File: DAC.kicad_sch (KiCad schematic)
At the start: 27 parts, among them J18 DAC_I2S, J19 DAC_OUT, J20 DAC_Amplified, J21 DAC_Amplified, J26 DAC_I2S, U6 PCM5100APW, U8 TL072

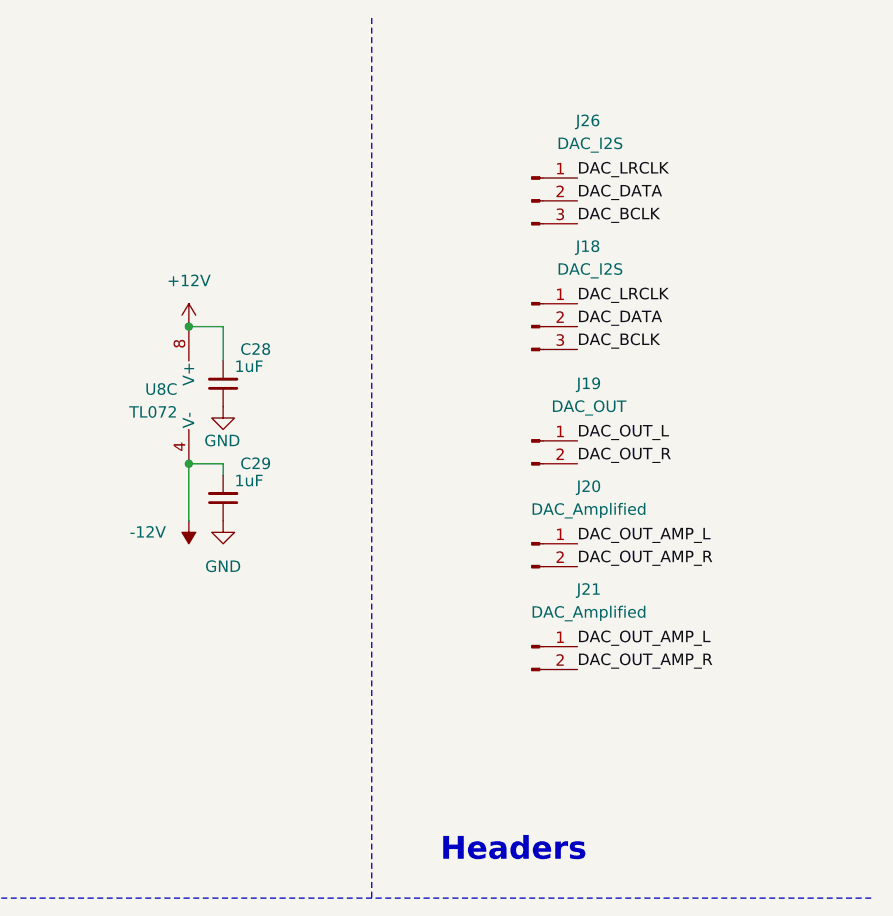
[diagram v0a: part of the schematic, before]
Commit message: Layout tweaks
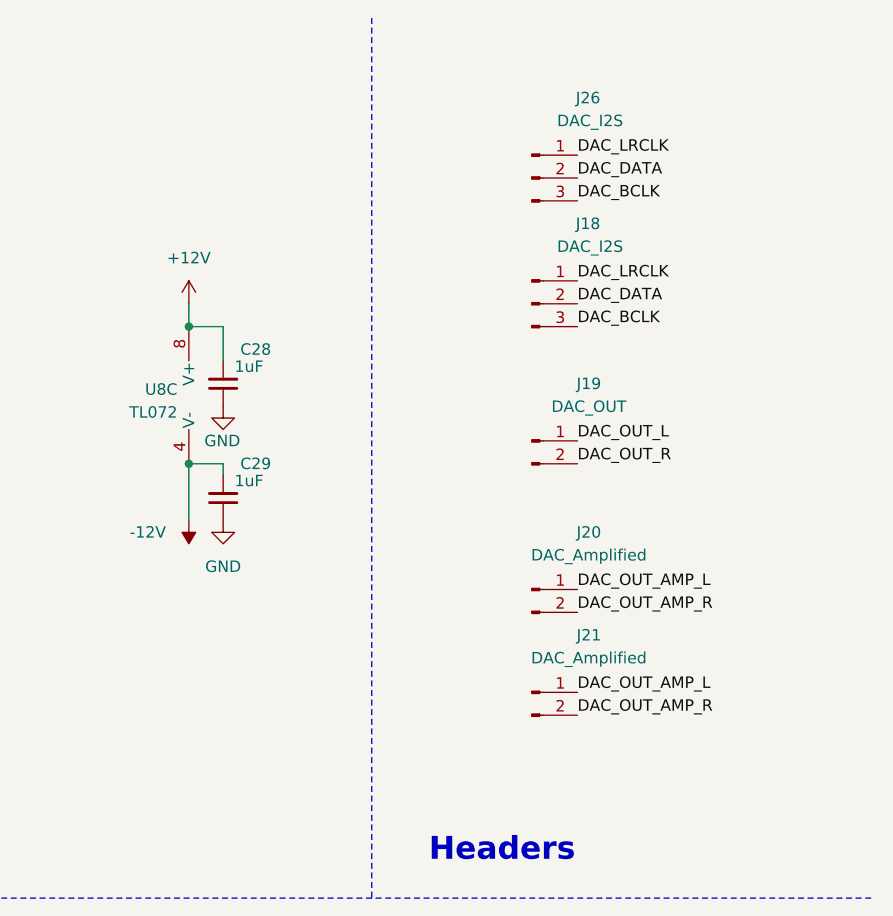
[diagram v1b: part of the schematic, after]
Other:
- moved on the sheet: J18, J20, J21, J26
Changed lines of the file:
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@@
+    (stroke (width 0) (type default))
+  )
+  (wire (pts (xy 208.28 44.45) (xy 208.28 46.99))
     (stroke (width 0) (type default))
   )
@@
     (stroke (width 0) (type default))
   )
-  (text "Headers" (at 236.22 106.68 0)
+  (text "Headers" (at 234.95 106.68 0)
     (effects (font (size 2.54 2.54) (thickness 0.508) bold) (justify left bottom))
   )
@@
     (effects (font (size 1.27 1.27)) (justify right bottom))
   )
-  (label "DAC_BCLK" (at 251.46 49.53 0) (fields_autoplaced)
-    (effects (font (size 1.27 1.27)) (justify left bottom))
-  )
-  (label "DAC_LRCLK" (at 251.46 30.48 0) (fields_autoplaced)
-    (effects (font (size 1.27 1.27)) (justify left bottom))
-  )
-  (label "DAC_DATA" (at 251.46 33.02 0) (fields_autoplaced)
+  (label "DAC_BCLK" (at 251.46 46.99 0) (fields_autoplaced)
+    (effects (font (size 1.27 1.27)) (justify left bottom))
+  )
+  (label "DAC_LRCLK" (at 251.46 27.94 0) (fields_autoplaced)
+    (effects (font (size 1.27 1.27)) (justify left bottom))
+  )
+  (label "DAC_DATA" (at 251.46 30.48 0) (fields_autoplaced)
     (effects (font (size 1.27 1.27)) (justify left bottom))
   )
@@
     (effects (font (size 1.27 1.27)) (justify right bottom))
   )
-  (label "DAC_OUT_AMP_R" (at 251.46 73.66 0) (fields_autoplaced)
+  (label "DAC_OUT_AMP_R" (at 251.46 78.74 0) (fields_autoplaced)
     (effects (font (size 1.27 1.27)) (justify left bottom))
   )
@@
     (effects (font (size 1.27 1.27)) (justify left bottom))
   )
-  (label "DAC_DATA" (at 251.46 46.99 0) (fields_autoplaced)
+  (label "DAC_DATA" (at 251.46 44.45 0) (fields_autoplaced)
     (effects (font (size 1.27 1.27)) (justify left bottom))
   )
@@
     (effects (font (size 1.27 1.27)) (justify right bottom))
   )
-  (label "DAC_OUT_AMP_R" (at 251.46 85.09 0) (fields_autoplaced)
-    (effects (font (size 1.27 1.27)) (justify left bottom))
-  )
-  (label "DAC_BCLK" (at 251.46 35.56 0) (fields_autoplaced)
-    (effects (font (size 1.27 1.27)) (justify left bottom))
-  )
-  (label "DAC_OUT_AMP_L" (at 251.46 71.12 0) (fields_autoplaced)
+  (label "DAC_OUT_AMP_R" (at 251.46 90.17 0) (fields_autoplaced)
+    (effects (font (size 1.27 1.27)) (justify left bottom))
+  )
+  (label "DAC_BCLK" (at 251.46 33.02 0) (fields_autoplaced)
+    (effects (font (size 1.27 1.27)) (justify left bottom))
+  )
+  (label "DAC_OUT_AMP_L" (at 251.46 76.2 0) (fields_autoplaced)
     (effects (font (size 1.27 1.27)) (justify left bottom))
   )
@@
     (effects (font (size 1.27 1.27)) (justify right bottom))
   )
-  (label "DAC_OUT_AMP_L" (at 251.46 82.55 0) (fields_autoplaced)
+  (label "DAC_OUT_AMP_L" (at 251.46 87.63 0) (fields_autoplaced)
     (effects (font (size 1.27 1.27)) (justify left bottom))
   )
@@
     (effects (font (size 1.27 1.27)) (justify left bottom))
   )
-  (label "DAC_LRCLK" (at 251.46 44.45 0) (fields_autoplaced)
+  (label "DAC_LRCLK" (at 251.46 41.91 0) (fields_autoplaced)
     (effects (font (size 1.27 1.27)) (justify left bottom))
   )
@@
     )
   )
-  (symbol (lib_id "Connector:Conn_01x03_Pin") (at 246.38 33.02 0) (unit 1)
-    (in_bom yes) (on_board yes) (dnp no)
-    (property "Reference" "J26" (at 254 24.13 0)
+  (symbol (lib_id "Connector:Conn_01x03_Pin") (at 246.38 30.48 0) (unit 1)
+    (in_bom yes) (on_board yes) (dnp no)
+    (property "Reference" "J26" (at 254 21.59 0)
       (effects (font (size 1.27 1.27)) (justify right))
     )
-    (property "Value" "DAC_I2S" (at 256.54 26.67 0)
+    (property "Value" "DAC_I2S" (at 256.54 24.13 0)
       (effects (font (size 1.27 1.27)) (justify right))
     )
-    (property "Footprint" "Connector_PinSocket_2.54mm:PinSocket_1x03_P2.54mm_Vertical" (at 246.38 33.02 0)
-      (effects (font (size 1.27 1.27)) hide)
-    )
-    (property "Datasheet" "~" (at 246.38 33.02 0)
+    (property "Footprint" "Connector_PinSocket_2.54mm:PinSocket_1x03_P2.54mm_Vertical" (at 246.38 30.48 0)
+      (effects (font (size 1.27 1.27)) hide)
+    )
+    (property "Datasheet" "~" (at 246.38 30.48 0)
       (effects (font (size 1.27 1.27)) hide)
     )
@@
     )
   )
-  (symbol (lib_id "Connector:Conn_01x02_Pin") (at 246.38 71.12 0) (unit 1)
-    (in_bom yes) (on_board yes) (dnp no)
-    (property "Reference" "J20" (at 252.73 64.77 0)
-      (effects (font (size 1.27 1.27)))
-    )
-    (property "Value" "DAC_Amplified" (at 252.73 67.31 0)
-      (effects (font (size 1.27 1.27)))
-    )
-    (property "Footprint" "Connector_PinSocket_2.54mm:PinSocket_1x02_P2.54mm_Vertical" (at 246.38 71.12 0)
-      (effects (font (size 1.27 1.27)) hide)
-    )
-    (property "Datasheet" "~" (at 246.38 71.12 0)
+  (symbol (lib_id "Connector:Conn_01x02_Pin") (at 246.38 76.2 0) (unit 1)
+    (in_bom yes) (on_board yes) (dnp no)
+    (property "Reference" "J20" (at 252.73 69.85 0)
+      (effects (font (size 1.27 1.27)))
+    )
+    (property "Value" "DAC_Amplified" (at 252.73 72.39 0)
+      (effects (font (size 1.27 1.27)))
+    )
+    (property "Footprint" "Connector_PinSocket_2.54mm:PinSocket_1x02_P2.54mm_Vertical" (at 246.38 76.2 0)
+      (effects (font (size 1.27 1.27)) hide)
+    )
+    (property "Datasheet" "~" (at 246.38 76.2 0)
       (effects (font (size 1.27 1.27)) hide)
     )
@@
     )
   )
-  (symbol (lib_id "power:+12V") (at 208.28 46.99 0) (unit 1)
+  (symbol (lib_id "power:+12V") (at 208.28 44.45 0) (unit 1)
     (in_bom yes) (on_board yes) (dnp no) (fields_autoplaced)
-    (property "Reference" "#PWR067" (at 208.28 50.8 0)
-      (effects (font (size 1.27 1.27)) hide)
-    )
-    (property "Value" "+12V" (at 208.28 41.91 0)
-      (effects (font (size 1.27 1.27)))
-    )
-    (property "Footprint" "" (at 208.28 46.99 0)
-      (effects (font (size 1.27 1.27)) hide)
-    )
-    (property "Datasheet" "" (at 208.28 46.99 0)
+    (property "Reference" "#PWR067" (at 208.28 48.26 0)
+      (effects (font (size 1.27 1.27)) hide)
+    )
+    (property "Value" "+12V" (at 208.28 39.37 0)
+      (effects (font (size 1.27 1.27)))
+    )
+    (property "Footprint" "" (at 208.28 44.45 0)
+      (effects (font (size 1.27 1.27)) hide)
+    )
+    (property "Datasheet" "" (at 208.28 44.45 0)
       (effects (font (size 1.27 1.27)) hide)
     )
@@
     )
   )
-  (symbol (lib_id "Connector:Conn_01x02_Pin") (at 246.38 82.55 0) (unit 1)
-    (in_bom yes) (on_board yes) (dnp no)
-    (property "Reference" "J21" (at 252.73 76.2 0)
-      (effects (font (size 1.27 1.27)))
-    )
-    (property "Value" "DAC_Amplified" (at 252.73 78.74 0)
-      (effects (font (size 1.27 1.27)))
-    )
-    (property "Footprint" "Connector_PinHeader_2.54mm:PinHeader_1x02_P2.54mm_Vertical" (at 246.38 82.55 0)
-      (effects (font (size 1.27 1.27)) hide)
-    )
-    (property "Datasheet" "~" (at 246.38 82.55 0)
+  (symbol (lib_id "Connector:Conn_01x02_Pin") (at 246.38 87.63 0) (unit 1)
+    (in_bom yes) (on_board yes) (dnp no)
+    (property "Reference" "J21" (at 252.73 81.28 0)
+      (effects (font (size 1.27 1.27)))
+    )
+    (property "Value" "DAC_Amplified" (at 252.73 83.82 0)
+      (effects (font (size 1.27 1.27)))
+    )
+    (property "Footprint" "Connector_PinHeader_2.54mm:PinHeader_1x02_P2.54mm_Vertical" (at 246.38 87.63 0)
+      (effects (font (size 1.27 1.27)) hide)
+    )
+    (property "Datasheet" "~" (at 246.38 87.63 0)
       (effects (font (size 1.27 1.27)) hide)
     )
@@
     )
   )
-  (symbol (lib_id "Connector:Conn_01x03_Pin") (at 246.38 46.99 0) (unit 1)
-    (in_bom yes) (on_board yes) (dnp no)
-    (property "Reference" "J18" (at 254 38.1 0)
+  (symbol (lib_id "Connector:Conn_01x03_Pin") (at 246.38 44.45 0) (unit 1)
+    (in_bom yes) (on_board yes) (dnp no)
+    (property "Reference" "J18" (at 254 35.56 0)
       (effects (font (size 1.27 1.27)) (justify right))
     )
-    (property "Value" "DAC_I2S" (at 256.54 40.64 0)
+    (property "Value" "DAC_I2S" (at 256.54 38.1 0)
       (effects (font (size 1.27 1.27)) (justify right))
     )
-    (property "Footprint" "Connector_PinHeader_2.54mm:PinHeader_1x03_P2.54mm_Vertical" (at 246.38 46.99 0)
-      (effects (font (size 1.27 1.27)) hide)
-    )
-    (property "Datasheet" "~" (at 246.38 46.99 0)
-      (effects (font (size 1.27 1.27)) hide)
-    )
+    (property "Footprint" "Connector_PinHeader_2.54mm:PinHeader_1x03_P2.54mm_Vertical" (at 246.38 44.45 0)
+      (effects (font (size 1.27 1.27)) hide)
+    )
+    (property "Datasheet" "~" (at 246.38 44.45 0)
+      (effects (font (size 1.27 1.27)) hide)
+    )

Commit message: Preparing for production
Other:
- moved on the sheet: C23
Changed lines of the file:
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@@
   (junction (at 76.2 36.83) (diameter 0) (color 0 0 0 0)
+  )
+  (junction (at 29.21 36.83) (diameter 0) (color 0 0 0 0)
   )
   (junction (at 149.86 69.85) (diameter 0) (color 0 0 0 0)
@@
     (stroke (width 0) (type default))
   )
+  (wire (pts (xy 64.77 27.94) (xy 64.77 29.21))
+    (stroke (width 0) (type default))
+  )
   (wire (pts (xy 166.37 34.29) (xy 166.37 44.45))
     (stroke (width 0) (type default))
@@
     (stroke (width 0) (type default))
   )
-  (wire (pts (xy 39.37 36.83) (xy 39.37 38.1))
+  (wire (pts (xy 29.21 36.83) (xy 29.21 38.1))
     (stroke (width 0) (type default))
   )
@@
     (stroke (width 0) (type default))
   )
+  (wire (pts (xy 83.82 66.04) (xy 74.93 66.04))
+    (stroke (width 0) (type default))
+  )
   (wire (pts (xy 156.21 26.67) (xy 149.86 26.67))
     (stroke (width 0) (type default))
@@
     (stroke (width 0) (type default))
   )
-  (wire (pts (xy 74.93 66.04) (xy 78.74 66.04))
-    (stroke (width 0) (type default))
-  )
   (wire (pts (xy 76.2 36.83) (xy 81.28 36.83))
     (stroke (width 0) (type default))
   )
-  (wire (pts (xy 83.82 66.04) (xy 87.63 66.04))
+  (wire (pts (xy 83.82 74.93) (xy 83.82 76.2))
     (stroke (width 0) (type default))
   )
@@
     (stroke (width 0) (type default))
   )
+  (wire (pts (xy 59.69 27.94) (xy 59.69 29.21))
+    (stroke (width 0) (type default))
+  )
   (wire (pts (xy 212.09 46.99) (xy 212.09 50.8))
     (stroke (width 0) (type default))
   )
   (wire (pts (xy 29.21 36.83) (xy 39.37 36.83))
+    (stroke (width 0) (type default))
+  )
+  (wire (pts (xy 83.82 69.85) (xy 83.82 66.04))
     (stroke (width 0) (type default))
   )
@@
     )
   )
-  (symbol (lib_id "power:+3.3VA") (at 59.69 29.21 0) (unit 1)
-    (in_bom yes) (on_board yes) (dnp no)
-    (property "Reference" "#PWR061" (at 59.69 33.02 0)
-      (effects (font (size 1.27 1.27)) hide)
-    )
-    (property "Value" "+3.3VA" (at 53.34 24.13 0)
-      (effects (font (size 1.27 1.27)) (justify left))
-    )
-    (property "Footprint" "" (at 59.69 29.21 0)
-      (effects (font (size 1.27 1.27)) hide)
-    )
-    (property "Datasheet" "" (at 59.69 29.21 0)
+  (symbol (lib_id "power:+3.3VA") (at 59.69 27.94 0) (unit 1)
+    (in_bom yes) (on_board yes) (dnp no)
+    (property "Reference" "#PWR061" (at 59.69 31.75 0)
+      (effects (font (size 1.27 1.27)) hide)
+    )
+    (property "Value" "+3.3VA" (at 53.34 22.86 0)
+      (effects (font (size 1.27 1.27)) (justify left))
+    )
+    (property "Footprint" "" (at 59.69 27.94 0)
+      (effects (font (size 1.27 1.27)) hide)
+    )
+    (property "Datasheet" "" (at 59.69 27.94 0)
       (effects (font (size 1.27 1.27)) hide)
     )
@@
     )
   )
-  (symbol (lib_id "power:GND") (at 39.37 38.1 0) (unit 1)
-    (in_bom yes) (on_board yes) (dnp no)
-    (property "Reference" "#PWR024" (at 39.37 44.45 0)
-      (effects (font (size 1.27 1.27)) hide)
-    )
-    (property "Value" "GND" (at 39.497 42.4942 0)
-      (effects (font (size 1.27 1.27)))
-    )
-    (property "Footprint" "" (at 39.37 38.1 0)
-      (effects (font (size 1.27 1.27)) hide)
-    )
-    (property "Datasheet" "" (at 39.37 38.1 0)
+  (symbol (lib_id "power:GND") (at 29.21 38.1 0) (unit 1)
+    (in_bom yes) (on_board yes) (dnp no)
+    (property "Reference" "#PWR024" (at 29.21 44.45 0)
+      (effects (font (size 1.27 1.27)) hide)
+    )
+    (property "Value" "GND" (at 29.337 42.4942 0)
+      (effects (font (size 1.27 1.27)))
+    )
+    (property "Footprint" "" (at 29.21 38.1 0)
+      (effects (font (size 1.27 1.27)) hide)
+    )
+    (property "Datasheet" "" (at 29.21 38.1 0)
       (effects (font (size 1.27 1.27)) hide)
     )
@@
   (symbol (lib_id "Device:C_Small") (at 78.74 72.39 0) (unit 1)
     (in_bom yes) (on_board yes) (dnp no)
-    (property "Reference" "C21" (at 81.661 71.2216 0)
-      (effects (font (size 1.27 1.27)) (justify left))
-    )
-    (property "Value" "2.2uF" (at 81.661 73.533 0)
+    (property "Reference" "C21" (at 72.39 72.39 0)
+      (effects (font (size 1.27 1.27)) (justify left))
+    )
+    (property "Value" "2.2uF" (at 71.12 74.93 0)
       (effects (font (size 1.27 1.27)) (justify left))
     )
@@
   )
   (symbol (lib_id "Device:C_Small") (at 139.7 81.28 0) (unit 1)
-    (in_bom yes) (on_board yes) (dnp no)
-    (property "Reference" "C25" (at 134.62 81.28 0)
-      (effects (font (size 1.27 1.27)) (justify left))
-    )
-    (property "Value" "1nF" (at 134.62 83.82 0)
+    (in_bom yes) (on_board yes) (dnp no) (fields_autoplaced)
+    (property "Reference" "C25" (at 142.24 80.6513 0)
+      (effects (font (size 1.27 1.27)) (justify left))
+    )
+    (property "Value" "1nF" (at 142.24 83.1913 0)
       (effects (font (size 1.27 1.27)) (justify left))
     )
@@
   )
   (symbol (lib_id "Device:C_Small") (at 139.7 45.72 0) (unit 1)
-    (in_bom yes) (on_board yes) (dnp no)
-    (property "Reference" "C24" (at 134.62 45.72 0)
-      (effects (font (size 1.27 1.27)) (justify left))
-    )
-    (property "Value" "1nF" (at 134.62 48.26 0)
+    (in_bom yes) (on_board yes) (dnp no) (fields_autoplaced)
+    (property "Reference" "C24" (at 142.24 45.0913 0)
+      (effects (font (size 1.27 1.27)) (justify left))
+    )
+    (property "Value" "1nF" (at 142.24 47.6313 0)
       (effects (font (size 1.27 1.27)) (justify left))
     )
@@
     )
   )
-  (symbol (lib_id "power:+3.3V") (at 64.77 29.21 0) (unit 1)
-    (in_bom yes) (on_board yes) (dnp no)
-    (property "Reference" "#PWR063" (at 64.77 33.02 0)
-      (effects (font (size 1.27 1.27)) hide)
-    )
-    (property "Value" "+3.3V" (at 66.04 24.13 0)
-      (effects (font (size 1.27 1.27)))
-    )
-    (property "Footprint" "" (at 64.77 29.21 0)
-      (effects (font (size 1.27 1.27)) hide)
-    )
-    (property "Datasheet" "" (at 64.77 29.21 0)
+  (symbol (lib_id "power:+3.3V") (at 64.77 27.94 0) (unit 1)
+    (in_bom yes) (on_board yes) (dnp no)
+    (property "Reference" "#PWR063" (at 64.77 31.75 0)
+      (effects (font (size 1.27 1.27)) hide)
+    )
+    (property "Value" "+3.3V" (at 66.04 22.86 0)
+      (effects (font (size 1.27 1.27)))
+    )
+    (property "Footprint" "" (at 64.77 27.94 0)
+      (effects (font (size 1.27 1.27)) hide)
+    )
+    (property "Datasheet" "" (at 64.77 27.94 0)
       (effects (font (size 1.27 1.27)) hide)
     )
@@
     )
   )
-  (symbol (lib_id "power:GND") (at 87.63 66.04 90) (unit 1)
-    (in_bom yes) (on_board yes) (dnp no)
-    (property "Reference" "#PWR066" (at 93.98 66.04 0)
-      (effects (font (size 1.27 1.27)) hide)
-    )
-    (property "Value" "GND" (at 92.0242 65.913 0)
-      (effects (font (size 1.27 1.27)))
-    )
-    (property "Footprint" "" (at 87.63 66.04 0)
-      (effects (font (size 1.27 1.27)) hide)
-    )
-    (property "Datasheet" "" (at 87.63 66.04 0)
+  (symbol (lib_id "power:GND") (at 83.82 76.2 0) (unit 1)
+    (in_bom yes) (on_board yes) (dnp no)
+    (property "Reference" "#PWR066" (at 83.82 82.55 0)
+      (effects (font (size 1.27 1.27)) hide)
+    )
+    (property "Value" "GND" (at 83.947 80.5942 0)
+      (effects (font (size 1.27 1.27)))
+    )
+    (property "Footprint" "" (at 83.82 76.2 0)
+      (effects (font (size 1.27 1.27)) hide)
+    )
+    (property "Datasheet" "" (at 83.82 76.2 0)
       (effects (font (size 1.27 1.27)) hide)
     )
@@
     )
   )
-  (symbol (lib_id "Device:C_Small") (at 81.28 66.04 270) (unit 1)
-    (in_bom yes) (on_board yes) (dnp no)
-    (property "Reference" "C23" (at 85.09 60.96 90)
-      (effects (font (size 1.27 1.27)))
-    )
-    (property "Value" "100nF" (at 85.09 63.5 90)
-      (effects (font (size 1.27 1.27)))
-    )
-    (property "Footprint" "Capacitor_SMD:C_0805_2012Metric" (at 77.47 67.0052 0)
-      (effects (font (size 1.27 1.27)) hide)
-    )
-    (property "Datasheet" "~" (at 81.28 66.04 0)
-      (effects (font (size 1.27 1.27)) hide)
-    )
-    (property "Part_Number" "C14663" (at 81.28 66.04 0)
-      (effects (font (size 1.27 1.27)) hide)
-    )
+  (symbol (lib_id "Device:C_Small") (at 83.82 72.39 180) (unit 1)
+    (in_bom yes) (on_board yes) (dnp no) (fields_autoplaced)
+    (property "Reference" "C23" (at 86.36 71.7486 0)
+      (effects (font (size 1.27 1.27)) (justify right))
+    )
+    (property "Value" "100nF" (at 86.36 74.2886 0)
+      (effects (font (size 1.27 1.27)) (justify right))
+    )
+    (property "Footprint" "Capacitor_SMD:C_0805_2012Metric" (at 82.8548 68.58 0)
+      (effects (font (size 1.27 1.27)) hide)
+    )
+    (property "Datasheet" "~" (at 83.82 72.39 0)
+      (effects (font (size 1.27 1.27)) hide)
+    )
+    (property "Part_Number" "C14663" (at 83.82 72.39 0)
+      (effects (font (size 1.27 1.27)) hide)
+    )
